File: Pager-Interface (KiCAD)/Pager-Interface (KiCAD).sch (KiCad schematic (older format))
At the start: 20 parts, among them J1 USB_B_Micro, J2 SMA ANT, Q1 BC817, Q2 BC817, U1 AMS1117-3.3, U2 CP2102N-A01-GQFN24, U3 SI4432-Module, U4 ESP32-WROOM

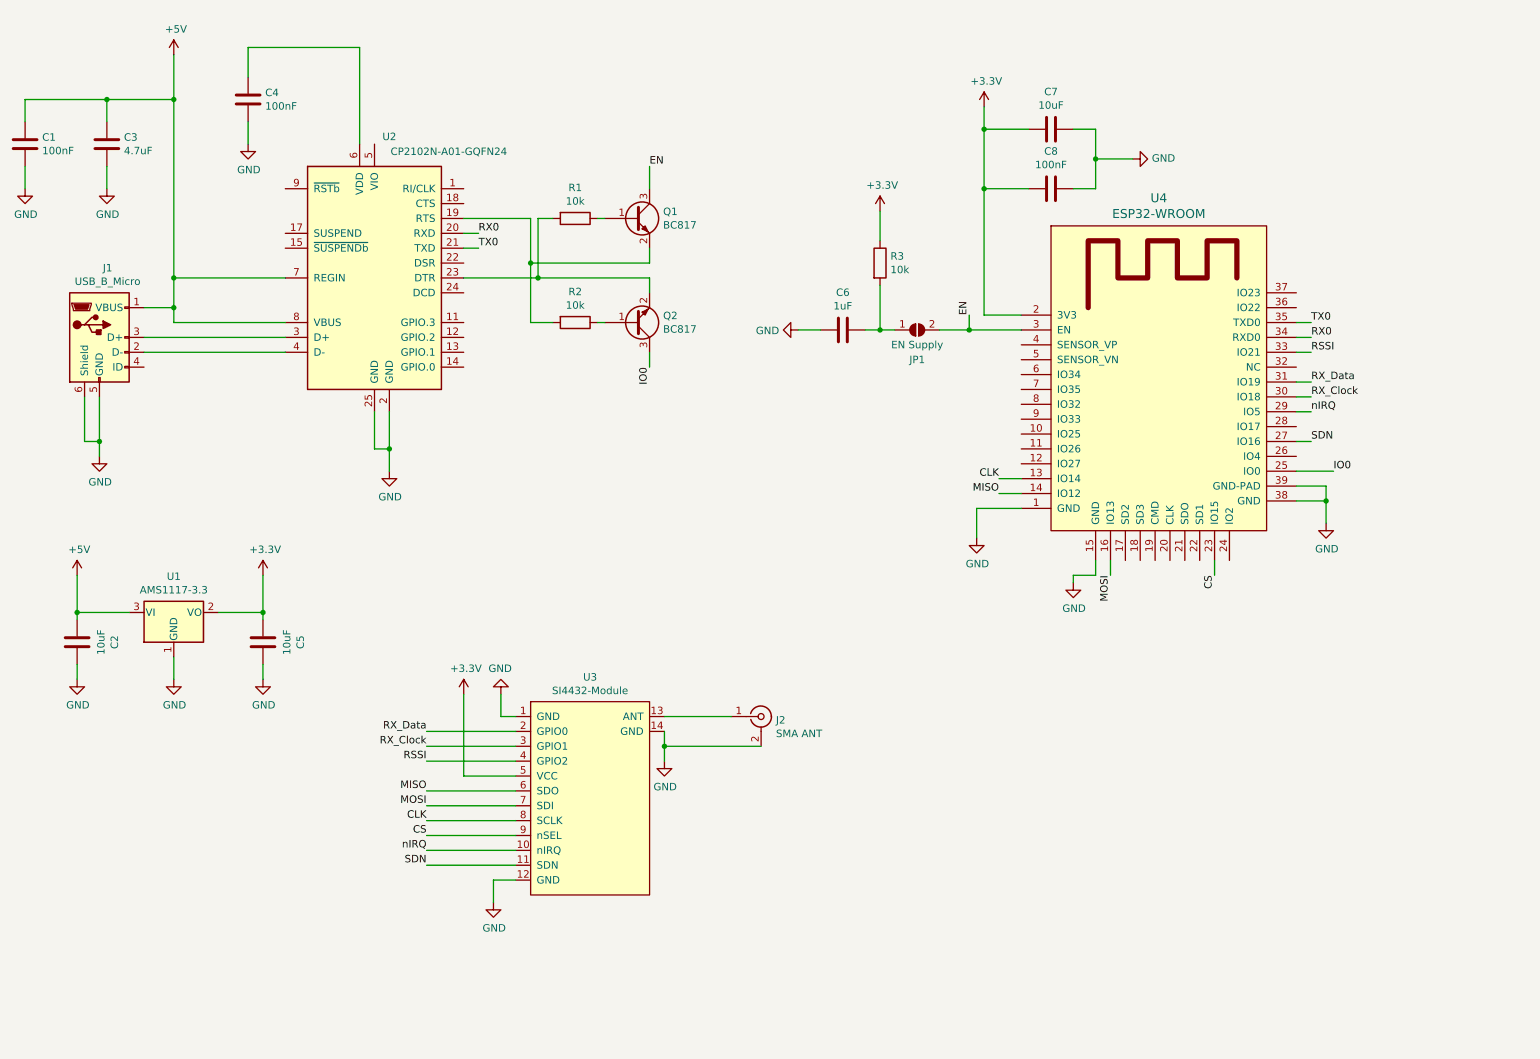
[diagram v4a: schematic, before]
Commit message: changed part numbers -> cp2102 to gqfn28 footprint + created outputfile for jlcpcb + some more silk text
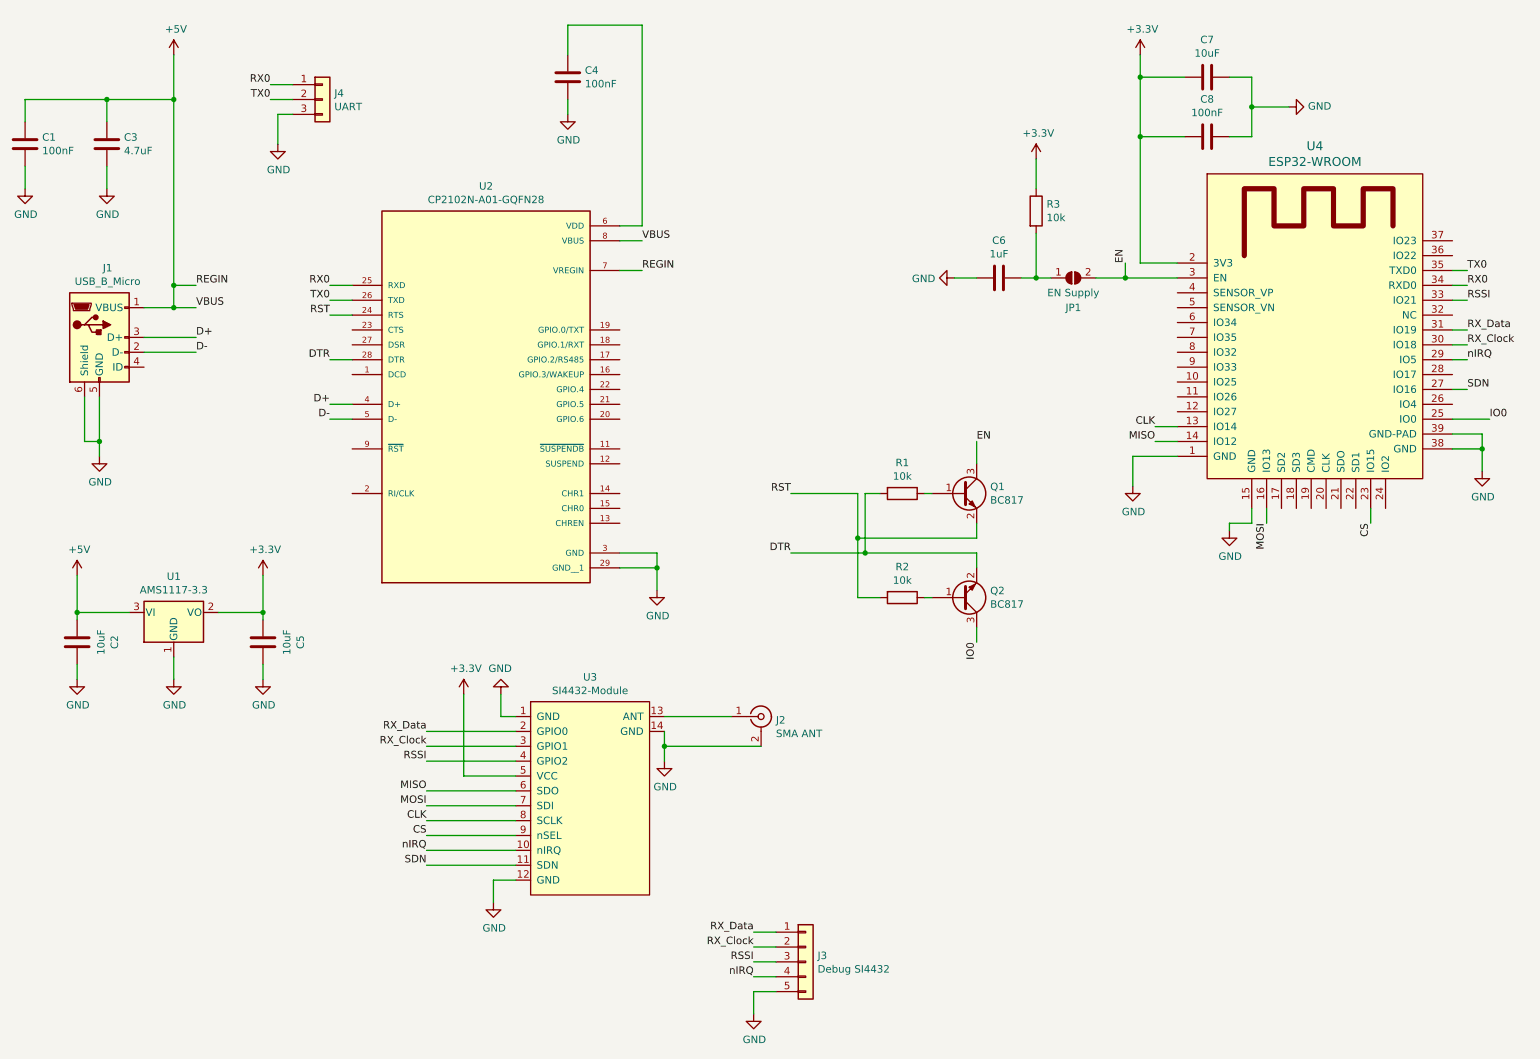
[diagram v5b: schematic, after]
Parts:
- removed U2: CP2102N-A01-GQFN24, Package_DFN_QFN:QFN-24-1EP_4x4mm_P0.5mm_EP2.6x2.6mm, symbol Interface_USB:CP2102N-A01-GQFN24
- added J3: Debug SI4432, Connector_PinHeader_2.54mm:PinHeader_1x05_P2.54mm_Vertical, symbol Connector_Generic:Conn_01x05
- added J4: UART, Connector_PinHeader_2.54mm:PinHeader_1x03_P2.54mm_Vertical, symbol Connector_Generic:Conn_01x03
- added U2: CP2102N-A01-GQFN28, CP2102:CP2102-GQFN28, symbol CP2102N-A01-GQFN28:CP2102N-A01-GQFN28
- C1, C4, C8: LCSC (none) -> C62912
- C2, C5, C7: LCSC (none) -> C15850
- C3: LCSC (none) -> C1746
- C6: LCSC (none) -> C282736
- J1: JCLC https://lcsc.com/product-detail/USB-Connectors_Shenzhen-Kin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 -> (none); Shop (none) -> https://lcsc.com/product-detail/USB-Connectors_Shenzhen-Kin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
- J2: JCLC https://lcsc.com/product-detail/RF-Connectors-Coaxial-Conne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 -> (none); Shop (none) -> C976230
- Q1, Q2: LCSC (none) -> C8589
- R1, R2: LCSC (none) -> C36231
- R3: LCSC (none) -> C17414
- U1: LCSC (none) -> C6186
- U4: LCSC (none) -> C82899
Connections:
- net +5V: now also U2.7 (VREGIN), U2.8 (VBUS)
- net GND: now also J3.5 (Pin_5), J4.3 (Pin_3), U2.29 (GND__1), U2.3 (GND)
- net RSSI: now also J3.3 (Pin_3)
- net RX0: now also J4.1 (Pin_1), U2.25 (RXD)
- net RX_Clock: now also J3.2 (Pin_2)
- net RX_Data: now also J3.1 (Pin_1)
- net TX0: now also J4.2 (Pin_2), U2.26 (TXD)
- net nIRQ: now also J3.4 (Pin_4)
- net D-: now reaches J1.2 (D-)
- net D-: now also U2.5 (D-)
- net D+: now reaches J1.3 (D+)
- net D+: now also U2.4 (D+)
- net RST: now reaches Q1.2 (E), R2.2
- net RST: now also U2.24 (RTS)
- net DTR: now reaches Q2.2 (E), R1.2
- net DTR: now also U2.28 (DTR)
- net at C4.1: now also U2.6 (VDD)
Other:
- moved on the sheet: C4, C6, C7, C8, JP1, Q1, Q2, R1, R2, R3, U4

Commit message: Changed the PCB to use the NodeMCU, because it is just a prototype and won't be used in the future
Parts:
- removed C1, C4, C8: 100nF, Capacitor_SMD:C_0805_2012Metric_Pad1.15x1.40mm_HandSolder, symbol Device:C
- removed C2, C5, C7: 10uF, Capacitor_SMD:C_0805_2012Metric_Pad1.15x1.40mm_HandSolder, symbol Device:C
- removed C3: 4.7uF, Capacitor_SMD:C_0805_2012Metric_Pad1.15x1.40mm_HandSolder, symbol Device:C
- removed C6: 1uF, Capacitor_SMD:C_0805_2012Metric_Pad1.15x1.40mm_HandSolder, symbol Device:C
- removed J1: USB_B_Micro, Connector_USB:USB_Micro-B_GCT_USB3076-30-A, symbol Connector:USB_B_Micro
- removed J4: UART, Connector_PinHeader_2.54mm:PinHeader_1x03_P2.54mm_Vertical, symbol Connector_Generic:Conn_01x03
- removed JP1: EN Supply, Jumper:SolderJumper-2_P1.3mm_Open_Pad1.0x1.5mm, symbol Jumper:SolderJumper_2_Open
- removed Q1, Q2: BC817, Package_TO_SOT_SMD:SOT-23, symbol Transistor_BJT:BC817
- removed R1, R2, R3: 10k, Resistor_SMD:R_0805_2012Metric_Pad1.15x1.40mm_HandSolder, symbol Device:R
- removed U1: AMS1117-3.3, Package_TO_SOT_SMD:SOT-223-3_TabPin2, symbol Regulator_Linear:AMS1117-3.3
- removed U2: CP2102N-A01-GQFN28, CP2102:CP2102-GQFN28, symbol CP2102N-A01-GQFN28:CP2102N-A01-GQFN28
- removed U3: SI4432-Module, SI4432 Module:SI4432-Module, symbol si4432:SI4432-Module
- removed U4: ESP32-WROOM, ESP32:ESP32-WROOM, symbol ESP32:ESP32-WROOM
- added H1, H2, H3: M3, MountingHole:MountingHole_3.2mm_M3_DIN965_Pad_TopBottom, symbol Mechanical:MountingHole_Pad
- added J1: VSPI, Connector_PinHeader_2.54mm:PinHeader_1x06_P2.54mm_Vertical, symbol Connector_Generic:Conn_01x06
- added J2: HSPI, Connector_PinHeader_2.54mm:PinHeader_1x06_P2.54mm_Vertical, symbol Connector_Generic:Conn_01x06
- added J3: Serial, Connector_PinHeader_2.54mm:PinHeader_1x04_P2.54mm_Vertical, symbol Connector_Generic:Conn_01x04
- added J4: Serial2, Connector_PinHeader_2.54mm:PinHeader_1x04_P2.54mm_Vertical, symbol Connector_Generic:Conn_01x04
- added J6: Ext Power, Connector_PinHeader_2.54mm:PinHeader_1x02_P2.54mm_Vertical, symbol Connector_Generic:Conn_01x02
- added J8: Power, Connector_PinHeader_2.54mm:PinHeader_1x02_P2.54mm_Vertical, symbol Connector_Generic:Conn_01x02
- added U1: ESP32_NodeMCU, Pager-Interface (KiCAD):ESP32_NodeMCU, symbol Pager-Interface_(KiCAD):ESP32_NodeMCU
- added U2: SI4432-Module, Pager-Interface (KiCAD):SI4432-Module, symbol Pager-Interface_(KiCAD):SI4432-Module
- J5: renamed from J2; footprint Connector_Coaxial:SMA_Amphenol_132289_EdgeMount -> Connector_Coaxial:SMA_Molex_73251-2120_EdgeMount_Horizontal
- renumbered J3 to J7
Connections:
- net labels added: HSPI_CLK, HSPI_CS, HSPI_MISO, HSPI_MOSI, RX2, TX2, VIN, VSPI_CLK, VSPI_CS, VSPI_MISO, VSPI_MOSI
- net labels removed: +5V, CLK, CS, D+, D-, DTR, EN, IO0, MISO, MOSI, REGIN, RST, VBUS
- wire segments 128 -> 86
